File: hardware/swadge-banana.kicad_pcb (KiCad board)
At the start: 2 copper layers, 82.7 x 128.1 mm, 54 parts, among them J1 USB_B_Micro, SW1 SW_SPDT, SW2 4-1437565-2, SW3 4-1437565-2, SW4 4-1437565-2, U1 GS321-TR, U2 AP1117-33, U4 ESP-13-WROOM-02D, U5 BUS_PCIexpress, U6 DISP_OLED_UG-2864HSWEG01, U9 QMA6981

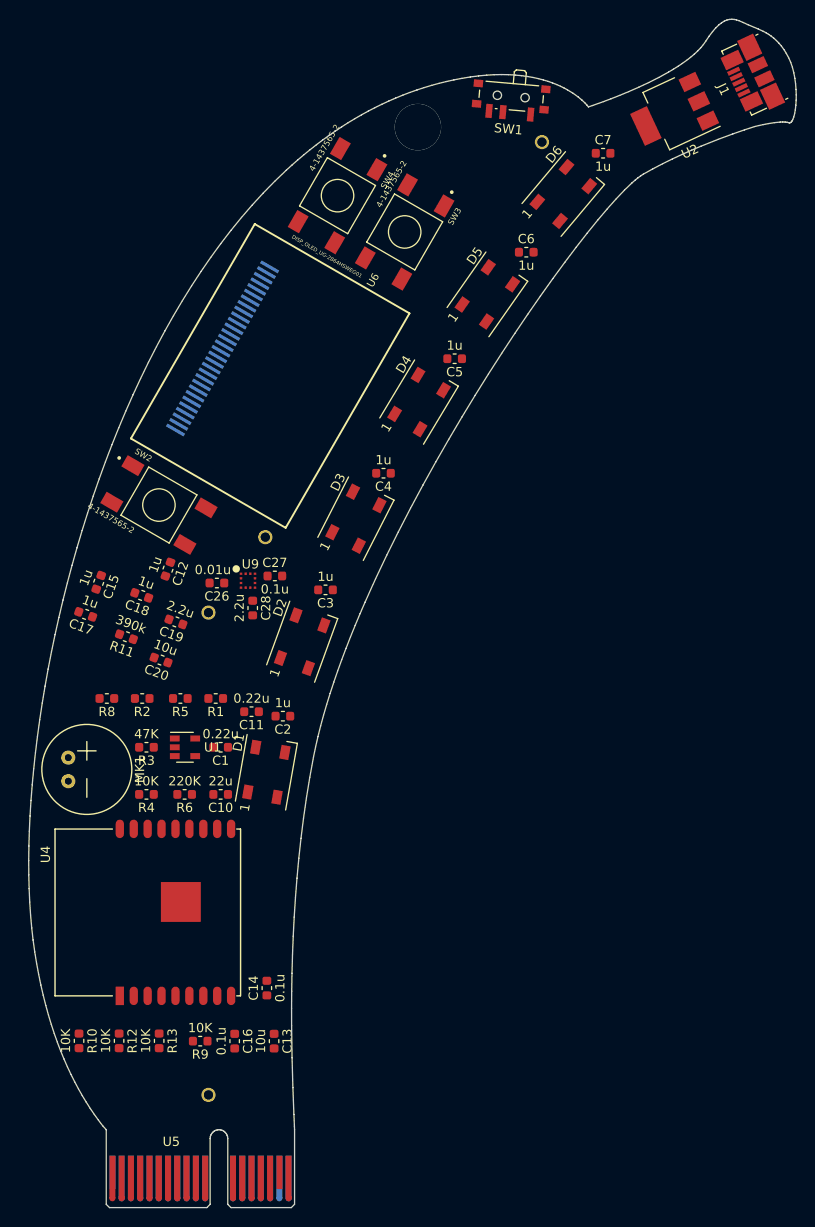
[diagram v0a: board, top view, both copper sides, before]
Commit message: Reworked banana, started laying it out
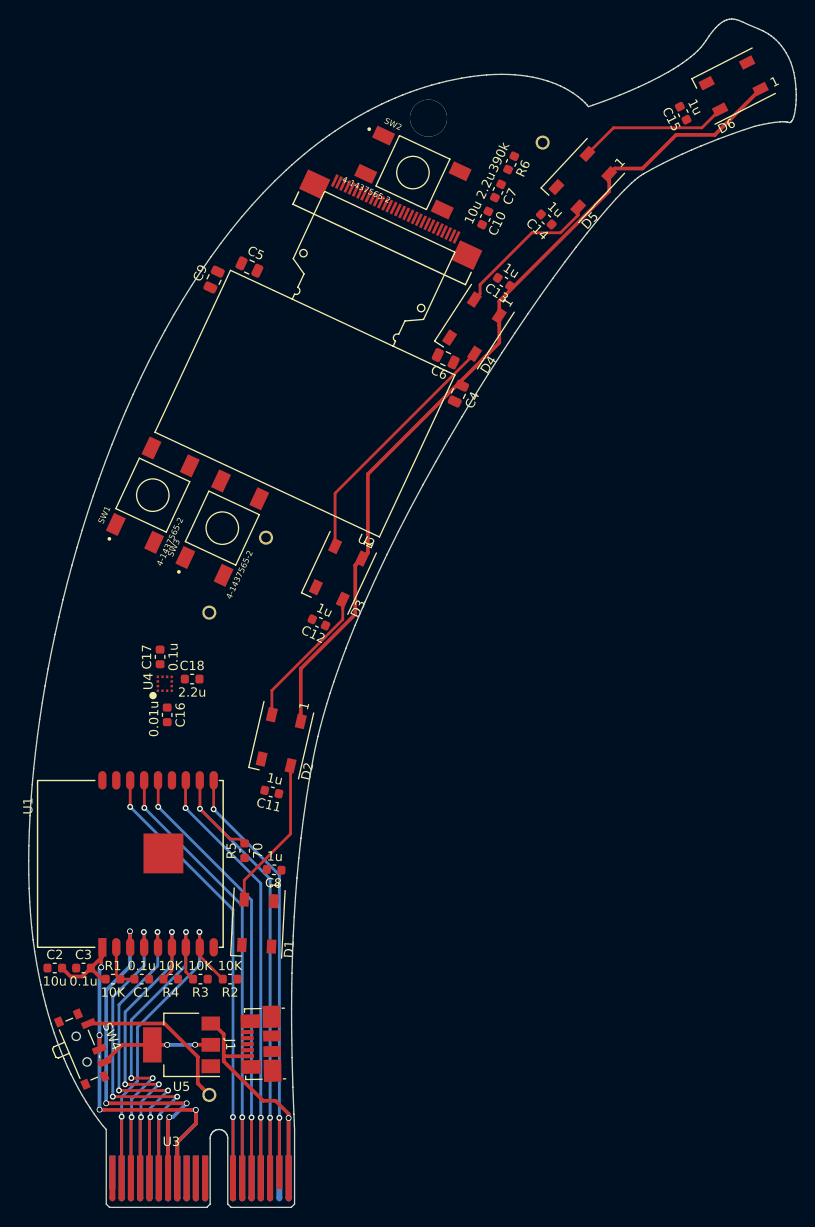
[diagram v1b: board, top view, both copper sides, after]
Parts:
- removed the C12 at (74.5, 84.6)
- removed the C13 at (86.0, 135.4)
- removed the C14 at (85.2, 129.7)
- removed the C15 at (67.1, 86.0)
- removed the C16 at (81.7, 135.4)
- removed the C17 at (65.7, 89.4)
- removed the C18 at (71.7, 87.4)
- removed C19: 2.2u, Swadge_Parts:C_0603_1608Metric
- removed C20: 10u, Swadge_Parts:C_0603_1608Metric
- removed MK1: Microphone, Swadge_Parts:CMA-4544PF-W
- removed R10, R12, R13, R8, R9: 10K, Swadge_Parts:R_0603_1608Metric
- removed R11: 390k, Swadge_Parts:R_0603_1608Metric
- removed the SW3 at (100.1, 48.2)
- removed the U1 at (76.4, 103.8)
- removed U6: DISP_OLED_UG-2864HSWEG01, Swadge_Parts:microbuilder-UG-2864HSWEG01_0.96IN_WRAPAROUND
- added C2: 10u, Swadge_Parts:C_0603_1608Metric, F.Cu at (62.3, 127.6)
- added C4: 1u, Swadge_Parts:C_0805_2012Metric, F.Cu at (105.8, 65.6)
- added C5: 1u, Swadge_Parts:C_0805_2012Metric, F.Cu at (83.3, 52.0)
- added C6: 1u, Swadge_Parts:C_0805_2012Metric, F.Cu at (104.5, 61.9)
- added C7: 2.2u, Swadge_Parts:C_0603_1608Metric, F.Cu at (110.1, 43.8)
- added C9: 1u, Swadge_Parts:C_0805_2012Metric, F.Cu at (79.5, 53.3)
- added SW2: 4-1437565-2, Swadge_Parts:SW_4-1437565-2, F.Cu at (100.9, 41.8)
- added U2: DISP_OLED_UG-2864HSWEG01, Swadge_Parts:oled-flat, F.Cu at (93.4, 58.0)
- C1: value 0.22u -> 0.1u
- C10: value 22u -> 10u
- C11: value 0.22u -> 1u
- C3: value 1u -> 0.1u
- R1: value 1K -> 10K
- R2, R3: value 47K -> 10K
- R5: value 10K -> 70
- R6: value 220K -> 390k
- moved J1 116.9 mm to (84.6, 135.7), turned to 91 degrees
- moved U5 113.5 mm to (76.0, 135.8), turned to 180 degrees
- moved SW4 112.1 mm to (65.5, 136.2), turned to 293 degrees
- moved R6 76.6 mm to (111.5, 40.8), turned to 245 degrees
- moved C10 68.4 mm to (108.7, 46.7), turned to 245 degrees
- moved BT1 59.3 mm to (100.0, 59.8), turned to 235 degrees
- moved BT2 59.3 mm to (78.9, 115.2), turned to 270 degrees
- moved C3 48.4 mm to (65.4, 127.6), turned to 0 degrees
- moved SW3 37.9 mm to (80.4, 80.1), turned to 65 degrees
- moved R1 32.2 mm to (68.6, 128.8), turned to 0 degrees
- moved R2 31.7 mm to (81.2, 128.8)
- moved C1 26.4 mm to (71.7, 128.8)
- moved R3 25.7 mm to (78.0, 128.8)
- moved D6 21.7 mm to (135.5, 32.5), turned to 207 degrees
- moved R4 20.1 mm to (74.8, 128.8)
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- renumbered C4 to C12, C5 to C13, C6 to C14, C7 to C15, C26 to C16, C27 to C17, C28 to C18, C2 to C8, SW2 to SW1, SW4 to SW3, SW1 to SW4, U4 to U1, U5 to U3, U9 to U4, U2 to U5
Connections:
- C10 pad 2: Net-(C1-Pad2) -> Net-(C10-Pad2)
- C11 pad 1: Net-(C11-Pad1) -> +3V3
- C11 pad 2: Net-(C11-Pad2) -> GND
- C3 pad 1: +3V3 -> GND
- C3 pad 2: GND -> +3V3
- J1 pad 2: (no net) -> Net-(J1-Pad2)
- J1 pad 3: (no net) -> Net-(J1-Pad3)
- J1 pad 4: (no net) -> Net-(J1-Pad4)
- R1 pad 1: AUD_PWR -> +3V3
- R2 pad 1: Net-(R2-Pad1) -> +3V3
- R2 pad 2: Net-(C1-Pad2) -> SCL
- R3 pad 1: Net-(R2-Pad1) -> +3V3
- R3 pad 2: Net-(C11-Pad1) -> SDA
- R4 pad 1: Net-(R4-Pad1) -> GND
- R4 pad 2: Net-(C11-Pad1) -> _RES
- R5 pad 1: GND -> Net-(D1-Pad4)
- R5 pad 2: Net-(R2-Pad1) -> RX
- R6 pad 1: ADC_PIN -> GND
- R6 pad 2: Net-(R4-Pad1) -> Net-(R6-Pad2)
- U1 pad 2: Net-(C16-Pad2) -> Net-(C1-Pad2)
- U4 pad 10: (no net) -> Net-(U4-Pad10)
- U4 pad 11: (no net) -> Net-(U4-Pad11)
- U4 pad 5: (no net) -> Net-(U4-Pad5)
- U4 pad 6: (no net) -> Net-(U4-Pad6)
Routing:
- net +3V3: track 0.00 -> 146.3 mm, vias 0 -> 4
- net RX: track 0.00 -> 58.7 mm, vias 0 -> 2
- net ADC_PIN: track 0.00 -> 53.8 mm, vias 0 -> 2
- net REST: track 0.00 -> 53.6 mm, vias 0 -> 2
- net SW5: track 0.00 -> 53.3 mm, vias 0 -> 2
- net TX: track 0.00 -> 52.5 mm, vias 0 -> 2
- net SW4: track 0.00 -> 51.6 mm, vias 0 -> 2
- net AUD_PWR: track 0.00 -> 45.6 mm, vias 0 -> 4
- net _RES: track 0.00 -> 44.9 mm, vias 0 -> 4
- net SDA: track 0.00 -> 44.0 mm, vias 0 -> 4
- net SW3: track 0.00 -> 43.8 mm, vias 0 -> 4
- net SCL: track 0.00 -> 42.6 mm, vias 0 -> 2
- net SW2: track 0.00 -> 42.5 mm, vias 0 -> 4
- net +5V: track 0.00 -> 29.9 mm, vias 0 -> 1
- net Net-(D3-Pad2): track 0.00 -> 26.9 mm
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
